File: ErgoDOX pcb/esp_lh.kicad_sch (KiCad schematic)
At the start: 6 parts

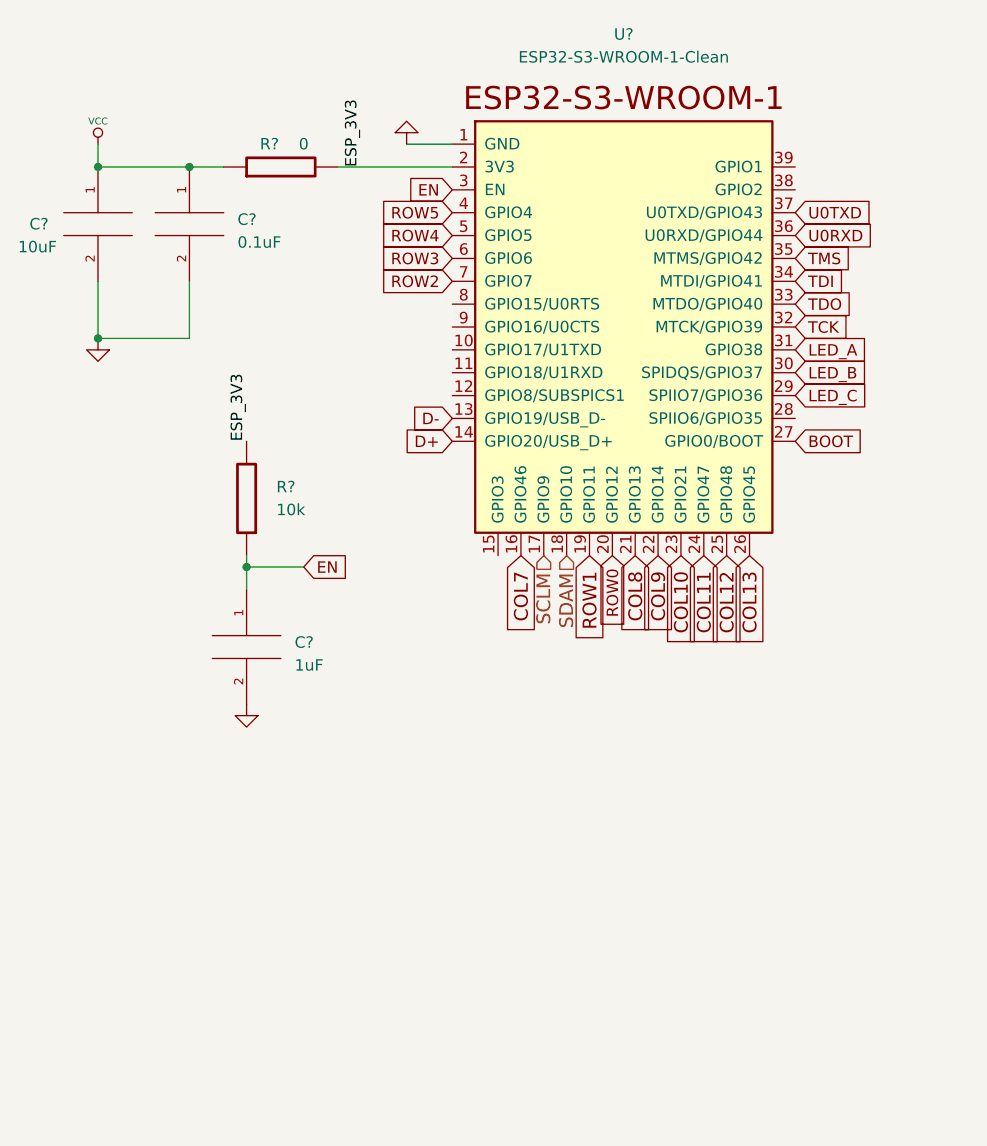
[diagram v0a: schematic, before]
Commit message: Create preliminary layout
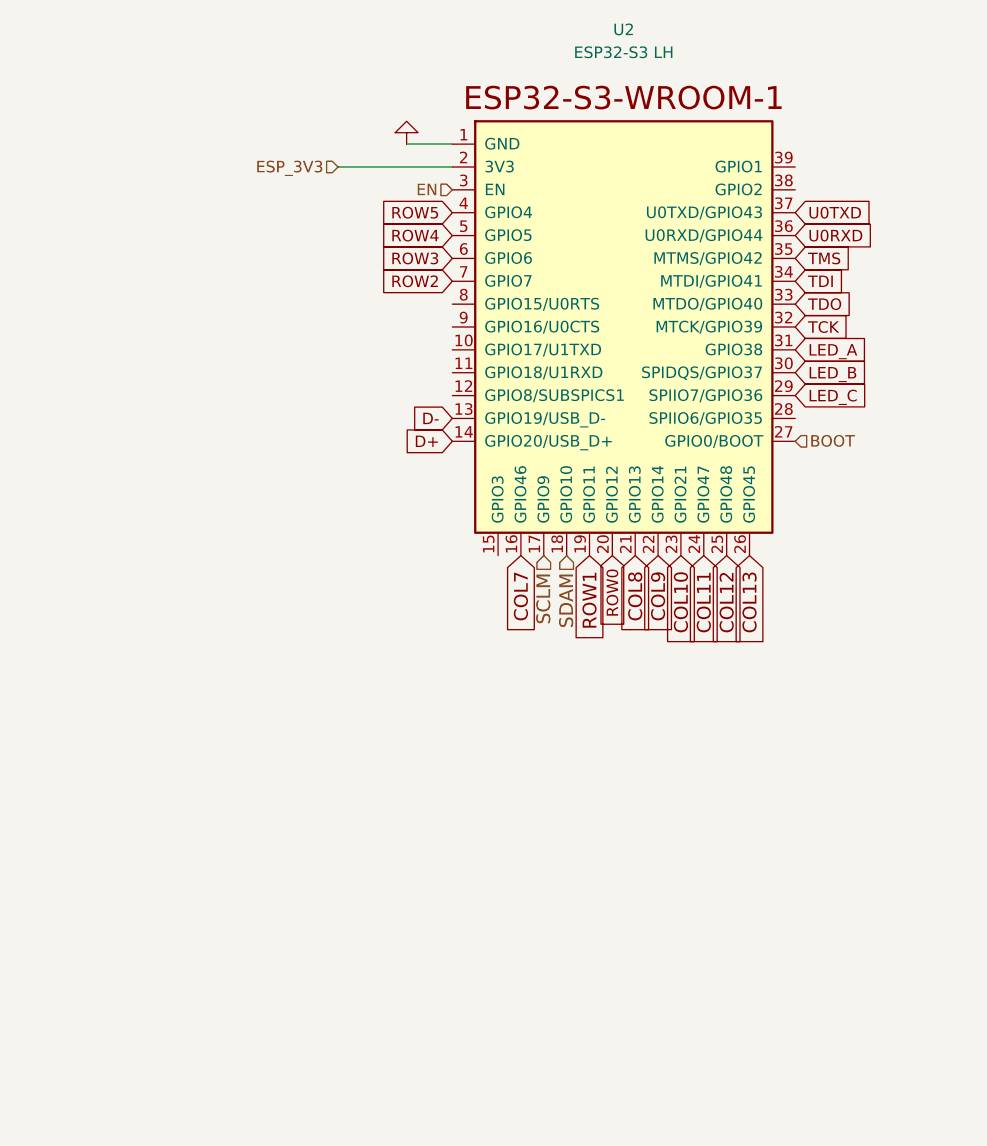
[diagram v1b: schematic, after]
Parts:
- removed C?: 0.1uF, symbol pspice:CAP
- removed C?: 1uF, symbol pspice:CAP
- removed C?: 10uF, symbol pspice:CAP
- removed R?: 0, symbol component:RESISTOR
- removed R?: 10k, symbol component:RESISTOR
- U2: renamed from U?; value ESP32-S3-WROOM-1-Clean -> ESP32-S3 LH
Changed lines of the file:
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@@
 (kicad_sch (version 20211123) (generator eeschema)
   (paper "A4")
-  (junction (at 125.73 71.12) (diameter 0) (color 0 0 0 0)
-  )
-  (junction (at 125.73 90.17) (diameter 0) (color 0 0 0 0)
-  )
-  (junction (at 135.89 71.12) (diameter 0) (color 0 0 0 0)
-  )
-  (junction (at 142.24 115.57) (diameter 0) (color 0 0 0 0)
-  )
   (wire (pts (xy 160.02 68.58) (xy 165.1 68.58))
     (stroke (width 0) (type default) (color 0 0 0 0))
   )
-  (wire (pts (xy 135.89 83.82) (xy 135.89 90.17))
-    (stroke (width 0) (type default) (color 0 0 0 0))
-  )
-  (wire (pts (xy 125.73 71.12) (xy 135.89 71.12))
-    (stroke (width 0) (type default) (color 0 0 0 0))
-  )
-  (wire (pts (xy 125.73 90.17) (xy 125.73 83.82))
-    (stroke (width 0) (type default) (color 0 0 0 0))
-  )
-  (wire (pts (xy 135.89 90.17) (xy 125.73 90.17))
-    (stroke (width 0) (type default) (color 0 0 0 0))
-  )
   (wire (pts (xy 152.4 71.12) (xy 165.1 71.12))
     (stroke (width 0) (type default) (color 0 0 0 0))
   )
-  (wire (pts (xy 142.24 115.57) (xy 148.59 115.57))
-    (stroke (width 0) (type default) (color 0 0 0 0))
-  )
-  (wire (pts (xy 142.24 114.3) (xy 142.24 115.57))
-    (stroke (width 0) (type default) (color 0 0 0 0))
-  )
-  (wire (pts (xy 135.89 71.12) (xy 139.7 71.12))
-    (stroke (width 0) (type default) (color 0 0 0 0))
-  )
-  (wire (pts (xy 142.24 115.57) (xy 142.24 118.11))
-    (stroke (width 0) (type default) (color 0 0 0 0))
-  )
-  (wire (pts (xy 125.73 68.58) (xy 125.73 71.12))
-    (stroke (width 0) (type default) (color 0 0 0 0))
-  )
-  (label "ESP_3V3" (at 142.24 101.6 90)
-    (effects (font (size 1.27 1.27)) (justify left bottom))
-  )
-  (label "ESP_3V3" (at 154.94 71.12 90)
-    (effects (font (size 1.27 1.27)) (justify left bottom))
-  )
   (global_label "COL8" (shape input) (at 185.42 114.3 270) (fields_autoplaced)
     (effects (font (size 1.524 1.524)) (justify right))
@@
     )
   )
-  (global_label "EN" (shape input) (at 148.59 115.57 0) (fields_autoplaced)
-    (effects (font (size 1.27 1.27)) (justify left))
-    (property "Intersheet References" "${INTERSHEET_REFS}" (id 0) (at 153.3937 115.4906 0)
-      (effects (font (size 1.27 1.27)) (justify left) hide)
-    )
-  )
   (global_label "COL9" (shape input) (at 187.96 114.3 270) (fields_autoplaced)
     (effects (font (size 1.524 1.524)) (justify right))
@@
     )
   )
-  (global_label "BOOT" (shape input) (at 203.2 101.6 0) (fields_autoplaced)
-    (effects (font (size 1.27 1.27)) (justify left))
-    (property "Intersheet References" "${INTERSHEET_REFS}" (id 0) (at 210.4228 101.5206 0)
-      (effects (font (size 1.27 1.27)) (justify left) hide)
-    )
-  )
   (global_label "COL13" (shape input) (at 198.12 114.3 270) (fields_autoplaced)
     (effects (font (size 1.524 1.524)) (justify right))
@@
     )
   )
-  (global_label "EN" (shape input) (at 165.1 73.66 180) (fields_autoplaced)
-    (effects (font (size 1.27 1.27)) (justify right))
-    (property "Intersheet References" "${INTERSHEET_REFS}" (id 0) (at 160.2963 73.5806 0)
-      (effects (font (size 1.27 1.27)) (justify right) hide)
-    )
-  )
   (global_label "D+" (shape input) (at 165.1 101.6 180) (fields_autoplaced)
     (effects (font (size 1.27 1.27)) (justify right))
@@
     )
   )
+  (hierarchical_label "BOOT" (shape input) (at 203.2 101.6 0)
+    (effects (font (size 1.27 1.27)) (justify left))
+  )
+  (hierarchical_label "EN" (shape input) (at 165.1 73.66 180)
+    (effects (font (size 1.27 1.27)) (justify right))
+  )
   (hierarchical_label "SCLM" (shape input) (at 175.26 114.3 270)
     (effects (font (size 1.524 1.524)) (justify right))
+  )
+  (hierarchical_label "ESP_3V3" (shape input) (at 152.4 71.12 180)
+    (effects (font (size 1.27 1.27)) (justify right))
   )
   (hierarchical_label "SDAM" (shape input) (at 177.8 114.3 270)
@@
   (symbol (lib_id "Espressif:ESP32-S3-WROOM-1-Clean") (at 184.15 83.82 0) (unit 1)
     (in_bom yes) (on_board yes) (fields_autoplaced)
-    (property "Reference" "U?" (id 0) (at 184.15 56.388 0))
-    (property "Value" "ESP32-S3-WROOM-1-Clean" (id 1) (at 184.15 58.928 0))
+    (property "Reference" "U2" (id 0) (at 184.15 55.88 0))
+    (property "Value" "ESP32-S3 LH" (id 1) (at 184.15 58.42 0))
     (property "Footprint" "Espressif:ESP32-S3-WROOM-1" (id 2) (at 184.15 129.54 0)
       (effects (font (size 1.27 1.27)) hide)
@@
     (pin "9")
   )
-  (symbol (lib_id "component:RESISTOR") (at 146.05 71.12 90) (unit 1)
-    (in_bom yes) (on_board yes)
-    (property "Reference" "R?" (id 0) (at 144.78 68.58 90))
-    (property "Value" "0" (id 1) (at 148.59 68.58 90))
-    (property "Footprint" "" (id 2) (at 146.05 71.12 0)
-      (effects (font (size 1.27 1.27)) hide)
-    )
-    (property "Datasheet" "" (id 3) (at 146.05 71.12 0)
-      (effects (font (size 1.27 1.27)) hide)
-    )
-    (pin "1")
-    (pin "2")
-  )
-  (symbol (lib_id "pspice:CAP") (at 135.89 77.47 0) (unit 1)
-    (in_bom yes) (on_board yes)
-    (property "Reference" "C?" (id 0) (at 141.224 76.9619 0)
-      (effects (font (size 1.27 1.27)) (justify left))
-    )
-    (property "Value" "0.1uF" (id 1) (at 141.224 79.5019 0)
-      (effects (font (size 1.27 1.27)) (justify left))
-    )
-    (property "Footprint" "" (id 2) (at 135.89 77.47 0)
-      (effects (font (size 1.27 1.27)) hide)
-    )
-    (property "Datasheet" "~" (id 3) (at 135.89 77.47 0)
-      (effects (font (size 1.27 1.27)) hide)
-    )
-    (pin "1")
-    (pin "2")
-  )
-  (symbol (lib_id "component:GND") (at 125.73 91.44 0) (mirror y) (unit 1)
-    (in_bom yes) (on_board yes)
-    (property "Reference" "#PWR?" (id 0) (at 125.73 91.44 0)
-      (effects (font (size 0.762 0.762)) hide)
-    )
-    (property "Value" "GND" (id 1) (at 125.73 93.218 0)
-      (effects (font (size 0.762 0.762)) hide)
-    )
-    (property "Footprint" "" (id 2) (at 125.73 91.44 0)
-      (effects (font (size 1.524 1.524)) hide)
-    )
-    (property "Datasheet" "" (id 3) (at 125.73 91.44 0)
-      (effects (font (size 1.524 1.524)) hide)
-    )
-    (pin "1")
-  )
-  (symbol (lib_id "component:RESISTOR") (at 142.24 107.95 180) (unit 1)
-    (in_bom yes) (on_board yes) (fields_autoplaced)
-    (property "Reference" "R?" (id 0) (at 145.542 106.6799 0)
-      (effects (font (size 1.27 1.27)) (justify right))
-    )
-    (property "Value" "10k" (id 1) (at 145.542 109.2199 0)
-      (effects (font (size 1.27 1.27)) (justify right))
-    )
-    (property "Footprint" "" (id 2) (at 142.24 107.95 0)
-      (effects (font (size 1.27 1.27)) hide)
-    )
-    (property "Datasheet" "" (id 3) (at 142.24 107.95 0)
-      (effects (font (size 1.27 1.27)) hide)
-    )
-    (pin "1")
-    (pin "2")
-  )
-  (symbol (lib_id "component:VCC") (at 125.73 68.58 0) (unit 1)
-    (in_bom yes) (on_board yes)
-    (property "Reference" "#PWR?" (id 0) (at 125.73 66.04 0)
-      (effects (font (size 0.762 0.762)) hide)
-    )
-    (property "Value" "VCC" (id 1) (at 125.73 66.04 0)
-      (effects (font (size 0.762 0.762)))
-    )
-    (property "Footprint" "" (id 2) (at 125.73 68.58 0)
-      (effects (font (size 1.524 1.524)) hide)
-    )
-    (property "Datasheet" "" (id 3) (at 125.73 68.58 0)
-      (effects (font (size 1.524 1.524)) hide)
-    )
-    (pin "1")
-  )
   (symbol (lib_id "component:GND") (at 160.02 67.31 0) (mirror x) (unit 1)
     (in_bom yes) (on_board yes)
-    (property "Reference" "#PWR?" (id 0) (at 160.02 67.31 0)
+    (property "Reference" "#PWR031" (id 0) (at 160.02 67.31 0)
       (effects (font (size 0.762 0.762)) hide)
     )
@@
       (effects (font (size 1.524 1.524)) hide)
     )
-    (pin "1")
-  )
-  (symbol (lib_id "pspice:CAP") (at 142.24 124.46 0) (unit 1)
-    (in_bom yes) (on_board yes)
-    (property "Reference" "C?" (id 0) (at 147.574 123.9519 0)
-      (effects (font (size 1.27 1.27)) (justify left))
-    )
-    (property "Value" "1uF" (id 1) (at 147.574 126.4919 0)
-      (effects (font (size 1.27 1.27)) (justify left))
-    )
-    (property "Footprint" "" (id 2) (at 142.24 124.46 0)
-      (effects (font (size 1.27 1.27)) hide)
-    )
-    (property "Datasheet" "~" (id 3) (at 142.24 124.46 0)
-      (effects (font (size 1.27 1.27)) hide)
-    )
-    (pin "1")
-    (pin "2")
-  )
-  (symbol (lib_id "pspice:CAP") (at 125.73 77.47 0) (unit 1)
-    (in_bom yes) (on_board yes)
-    (property "Reference" "C?" (id 0) (at 118.11 77.47 0)
-      (effects (font (size 1.27 1.27)) (justify left))
-    )
-    (property "Value" "10uF" (id 1) (at 116.84 80.01 0)
-      (effects (font (size 1.27 1.27)) (justify left))
-    )
-    (property "Footprint" "" (id 2) (at 125.73 77.47 0)
-      (effects (font (size 1.27 1.27)) hide)
-    )
-    (property "Datasheet" "~" (id 3) (at 125.73 77.47 0)
-      (effects (font (size 1.27 1.27)) hide)
-    )
-    (pin "1")
-    (pin "2")
-  )
-  (symbol (lib_id "component:GND") (at 142.24 132.08 0) (mirror y) (unit 1)
-    (in_bom yes) (on_board yes)
-    (property "Reference" "#PWR?" (id 0) (at 142.24 132.08 0)
-      (effects (font (size 0.762 0.762)) hide)
-    )
-    (property "Value" "GND" (id 1) (at 142.24 133.858 0)
-      (effects (font (size 0.762 0.762)) hide)
-    )
-    (property "Footprint" "" (id 2) (at 142.24 132.08 0)
-      (effects (font (size 1.524 1.524)) hide)
-    )
-    (property "Datasheet" "" (id 3) (at 142.24 132.08 0)
-      (effects (font (size 1.524 1.524)) hide)
-    )

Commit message: First route of board
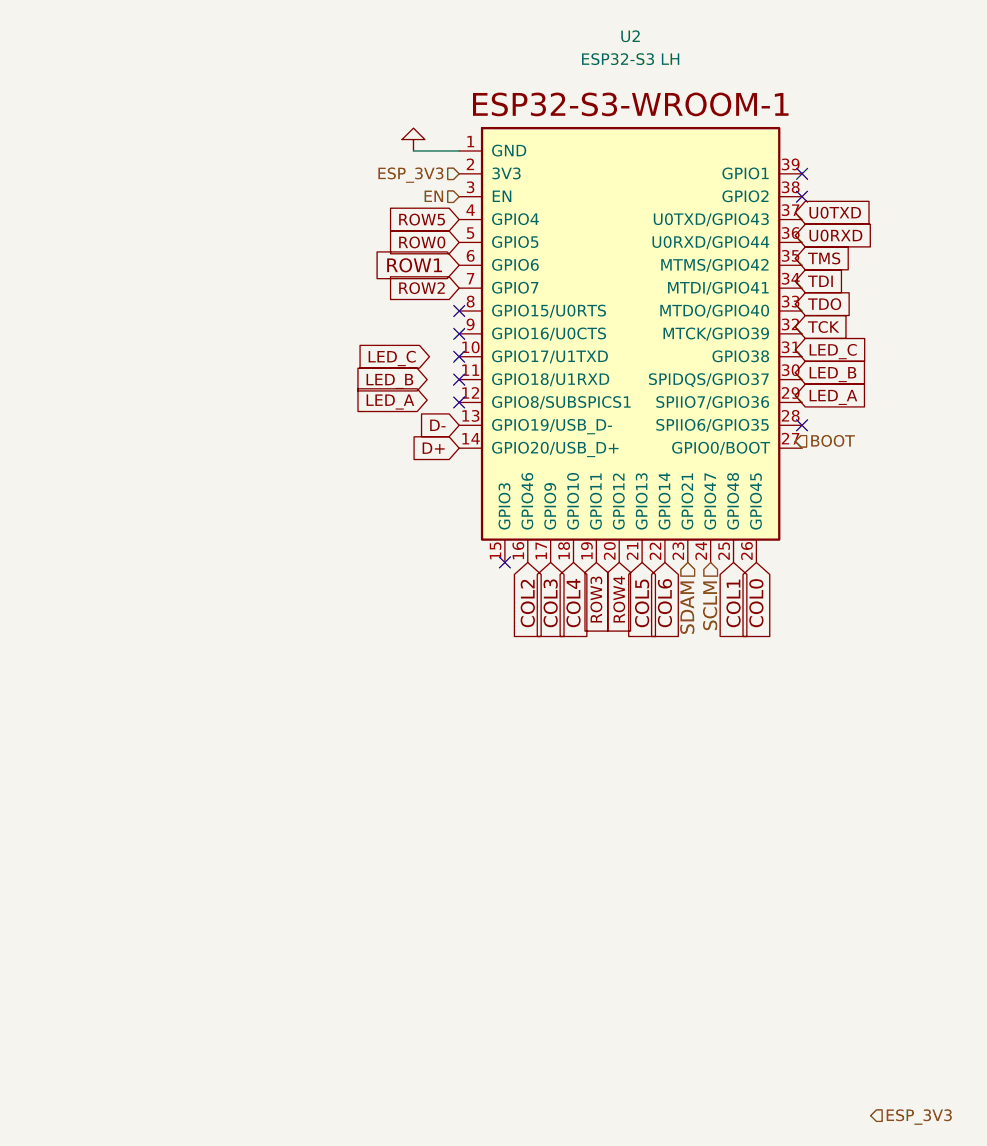
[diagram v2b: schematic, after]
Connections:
- net COL10 is gone; now on net SDAM: U2.23 (GPIO21)
- net COL11 is gone; now on net SCLM: U2.24 (GPIO47)
- net LED_A: now also U2.29 (SPIIO7/GPIO36); no longer U2.31 (GPIO38)
- net LED_C: now also U2.31 (GPIO38); no longer U2.29 (SPIIO7/GPIO36)
- net ROW0: now also U2.5 (GPIO5); no longer U2.20 (GPIO12)
- net ROW1: now also U2.6 (GPIO6); no longer U2.19 (GPIO11)
- net ROW3: now also U2.19 (GPIO11); no longer U2.6 (GPIO6)
- net ROW4: now also U2.20 (GPIO12); no longer U2.5 (GPIO5)
- net SCLM: no longer U2.17 (GPIO9)
- net SDAM: no longer U2.18 (GPIO10)
- net COL12 renamed COL1
- net COL13 renamed COL0
- net COL7 renamed COL2
- net COL8 renamed COL5
- net COL9 renamed COL6
- new net COL3: U2.17 (GPIO9)
- new net COL4: U2.18 (GPIO10)
- no-connect marks 0 -> 9
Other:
- moved on the sheet: U2
